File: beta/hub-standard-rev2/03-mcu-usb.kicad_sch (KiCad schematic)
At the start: 19 parts, among them U1 ESP32-S3-WROOM-1, U4 TPS3839K33

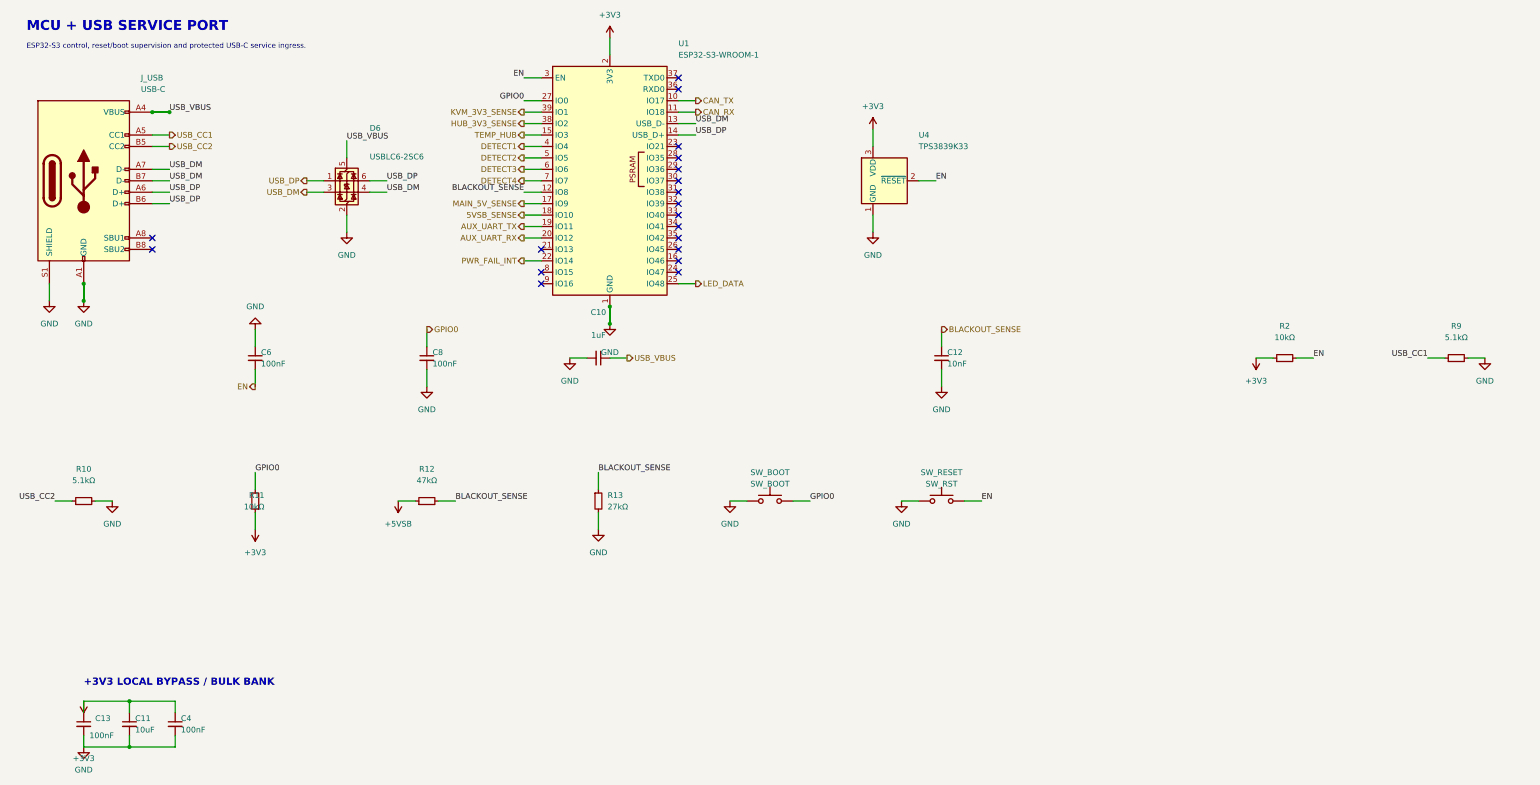
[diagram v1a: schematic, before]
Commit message: Rework BETA power rails and schematic composition
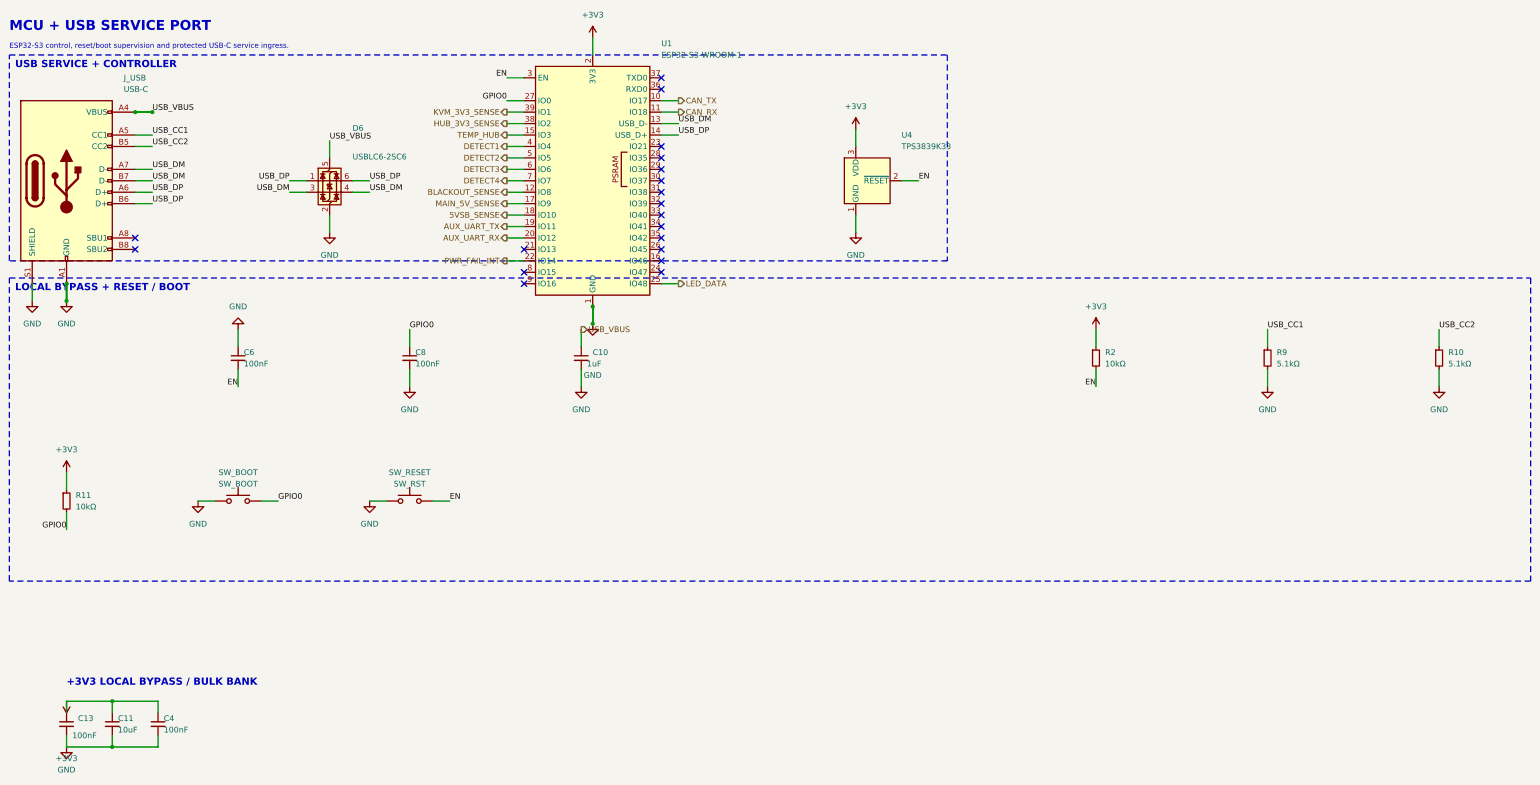
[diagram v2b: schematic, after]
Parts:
- removed C12: 10nF, cec-Capacitor_SMD:C_0402_1005Metric, symbol cec-vendor:C_Small
- removed R12: 47kΩ, cec-Resistor_SMD:R_0402_1005Metric, symbol cec-vendor:R_Small
- removed R13: 27kΩ, cec-Resistor_SMD:R_0402_1005Metric, symbol cec-vendor:R_Small
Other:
- note added: "LOCAL BYPASS + RESET / BOOT"
- note added: "USB SERVICE + CONTROLLER"

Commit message: Finalize compact Hub and ATX power-layout audit
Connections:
- net USB_DM renamed USB_D_N
- net USB_DP renamed USB_D_P
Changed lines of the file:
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@@
 	(label "USB_CC2" (at 76.2 88.9 0) (effects (font (size 1.27 1.27)) (justify left bottom)))
 	(label "USB_CC2" (at 361.95 129.54 0) (effects (font (size 1.27 1.27)) (justify left bottom)))
-	(label "USB_DM" (at 106.68 99.06 180) (effects (font (size 1.27 1.27)) (justify right bottom)))
-	(label "USB_DM" (at 124.46 99.06 0) (effects (font (size 1.27 1.27)) (justify left bottom)))
-	(label "USB_DM" (at 76.2 93.98 0) (effects (font (size 1.27 1.27)) (justify left bottom)))
-	(label "USB_DM" (at 76.2 96.52 0) (effects (font (size 1.27 1.27)) (justify left bottom)))
-	(label "USB_DM" (at 193.04 83.82 0) (effects (font (size 1.27 1.27)) (justify left bottom)))
-	(label "USB_DP" (at 106.68 96.52 180) (effects (font (size 1.27 1.27)) (justify right bottom)))
-	(label "USB_DP" (at 124.46 96.52 0) (effects (font (size 1.27 1.27)) (justify left bottom)))
-	(label "USB_DP" (at 76.2 99.06 0) (effects (font (size 1.27 1.27)) (justify left bottom)))
-	(label "USB_DP" (at 76.2 101.6 0) (effects (font (size 1.27 1.27)) (justify left bottom)))
-	(label "USB_DP" (at 193.04 86.36 0) (effects (font (size 1.27 1.27)) (justify left bottom)))
+	(label "USB_D_N" (at 106.68 99.06 180) (effects (font (size 1.27 1.27)) (justify right bottom)))
+	(label "USB_D_N" (at 124.46 99.06 0) (effects (font (size 1.27 1.27)) (justify left bottom)))
+	(label "USB_D_N" (at 76.2 93.98 0) (effects (font (size 1.27 1.27)) (justify left bottom)))
+	(label "USB_D_N" (at 76.2 96.52 0) (effects (font (size 1.27 1.27)) (justify left bottom)))
+	(label "USB_D_N" (at 193.04 83.82 0) (effects (font (size 1.27 1.27)) (justify left bottom)))
+	(label "USB_D_P" (at 106.68 96.52 180) (effects (font (size 1.27 1.27)) (justify right bottom)))
+	(label "USB_D_P" (at 124.46 96.52 0) (effects (font (size 1.27 1.27)) (justify left bottom)))
+	(label "USB_D_P" (at 76.2 99.06 0) (effects (font (size 1.27 1.27)) (justify left bottom)))
+	(label "USB_D_P" (at 76.2 101.6 0) (effects (font (size 1.27 1.27)) (justify left bottom)))
+	(label "USB_D_P" (at 193.04 86.36 0) (effects (font (size 1.27 1.27)) (justify left bottom)))
 	(label "USB_VBUS" (at 115.57 87.63 0) (effects (font (size 1.27 1.27)) (justify left bottom)))
 	(label "USB_VBUS" (at 76.2 81.28 0) (effects (font (size 1.27 1.27)) (justify left bottom)))

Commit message: pipeline: integrate route-aware physical design flow
Generalize critical-first placement and routing, future-congestion and power-authority planning, route provenance, process watchdogs, fab/thermal validation, dashboard review, and XFCN integration. Add the supporting board contracts, component libraries, documentation, and regression coverage.
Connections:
- net 5VSB_SENSE renamed PWR_SOURCE_STATUS
- net MAIN_5V_SENSE renamed 5V_SYS_SENSE
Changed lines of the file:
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@@
 	(label "USB_VBUS" (at 115.57 87.63 0) (effects (font (size 1.27 1.27)) (justify left bottom)))
 	(label "USB_VBUS" (at 76.2 81.28 0) (effects (font (size 1.27 1.27)) (justify left bottom)))
-	(hierarchical_label "5VSB_SENSE"
-		(shape output)
+	(hierarchical_label "PWR_SOURCE_STATUS"
+		(shape input)
 		(at 154.94 104.14 180)
 		(effects (font (size 1.27 1.27)) (justify right))
@@
 		(effects (font (size 1.27 1.27)) (justify left))
 	)
-	(hierarchical_label "MAIN_5V_SENSE"
+	(hierarchical_label "5V_SYS_SENSE"
 		(shape output)
 		(at 154.94 101.6 180)
